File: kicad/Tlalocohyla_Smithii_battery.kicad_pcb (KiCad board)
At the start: 2 copper layers, 85.2 x 29.4 mm, 3 parts

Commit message: Add filled zone
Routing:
- added copper zone on B.Cu, net (none)
- added copper zone on F.Cu, net (none)
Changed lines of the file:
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@@
   (gr_line (start 132.221213 98.455283) (end 167.778787 98.455283) (layer "Edge.Cuts") (width 0.15))
   (gr_arc (start 173.829848 107.809025) (mid 172.682891 107.758948) (end 171.90728 106.912517) (layer "Edge.Cuts") (width 0.15))
+  (zone (net 0) (net_name "") (layers F&B.Cu) (hatch edge 0.508)
+    (connect_pads (clearance 0.508))
+    (min_thickness 0.254) (filled_areas_thickness no)
+    (fill yes (thermal_gap 0.508) (thermal_bridge_width 0.508))
+    (polygon
+      (pts
+        (xy 193 129)
+        (xy 107 129)
+        (xy 107 98)
+        (xy 193 98)
+      )
+    )
+  )
 )

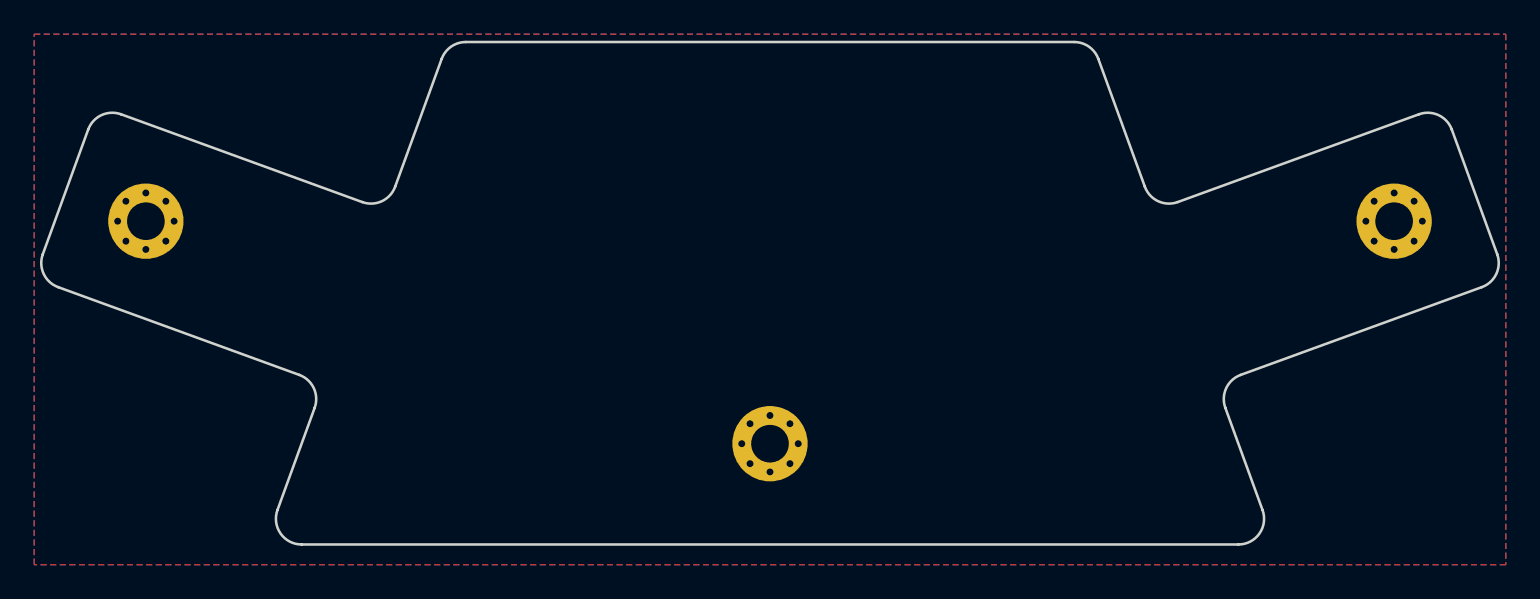
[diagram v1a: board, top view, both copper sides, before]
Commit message: Update battery and bottom PCB
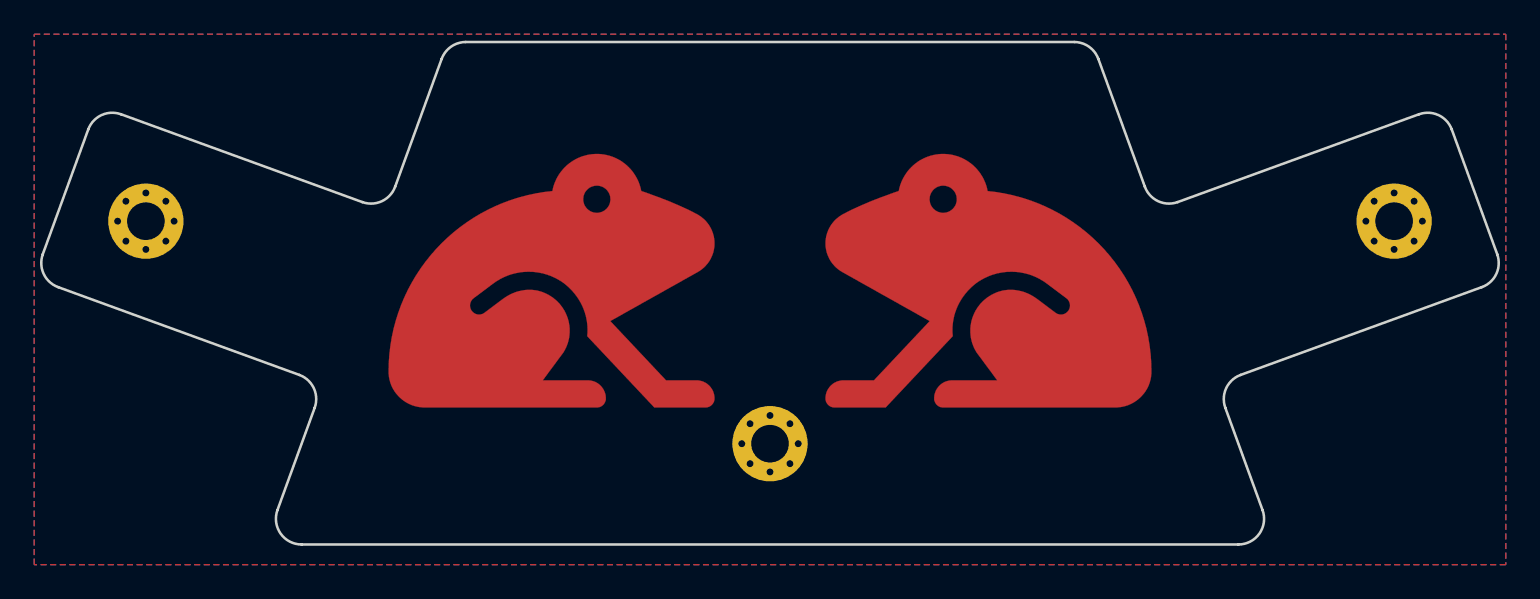
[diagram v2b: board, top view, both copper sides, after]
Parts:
- added G***: LOGO, Library:Frog Batt, F.Cu at (150.0, 115.0)
- added REF**: Leaves batt, Library:Leaves batt, F.Cu at (150.0, 121.0)

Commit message: Update battery and bottom PCB
- Adjusments
- New frog footprint
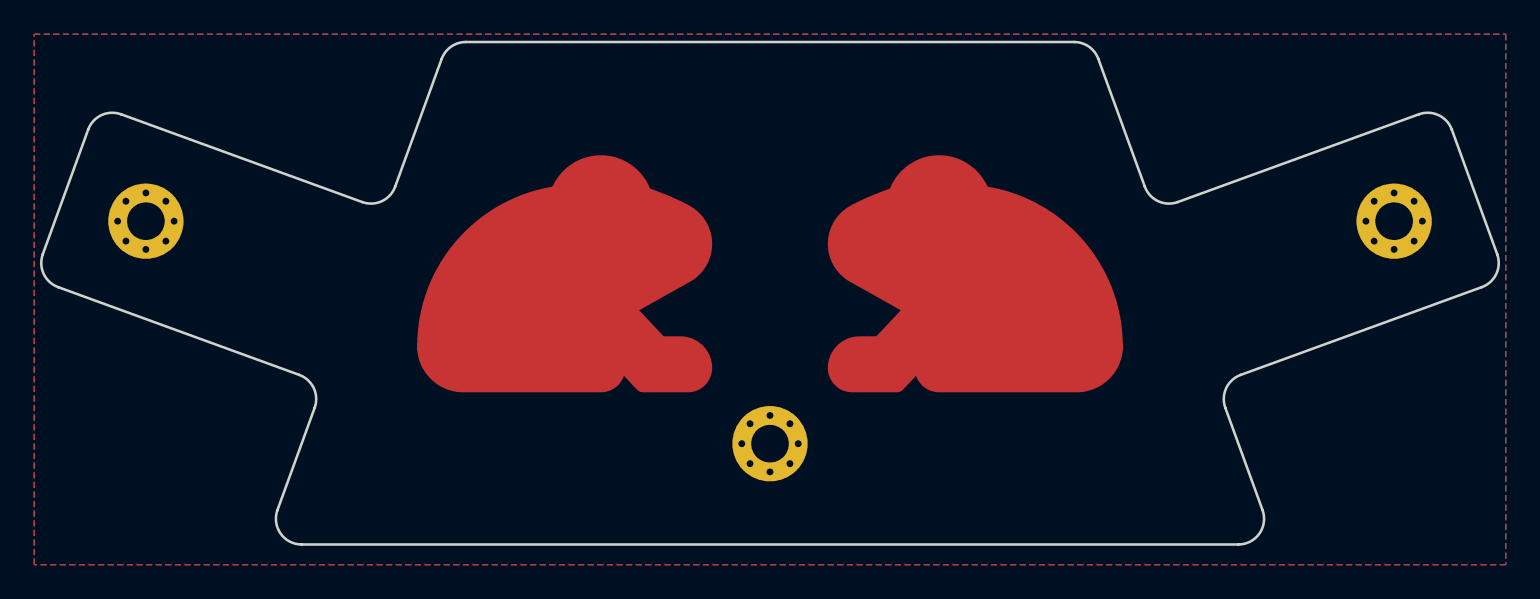
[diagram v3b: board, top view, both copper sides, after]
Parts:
- removed G***: LOGO, Library:Frog Batt
- added REF**: Frog Batt 2, Library:Frog Batt 2, F.Cu at (150.0, 112.0)
